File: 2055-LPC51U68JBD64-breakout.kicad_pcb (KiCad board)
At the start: 2 copper layers, 76.2 x 23.4 mm, 24 parts, among them J1 Conn_01x30, J2 Conn_01x30, J3 0548190519, U1 AZ1117CH-3.3TRG1, U2 LPC51U68

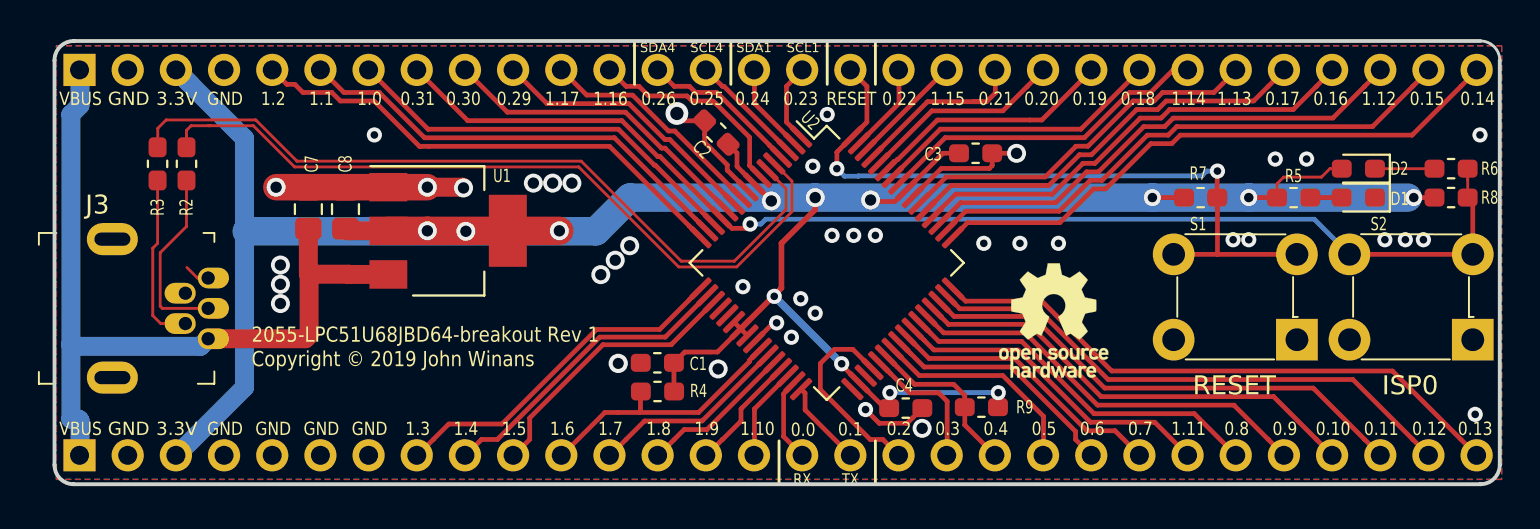
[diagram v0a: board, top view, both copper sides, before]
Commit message: Adjust edge cuts arc with wrong thickness.
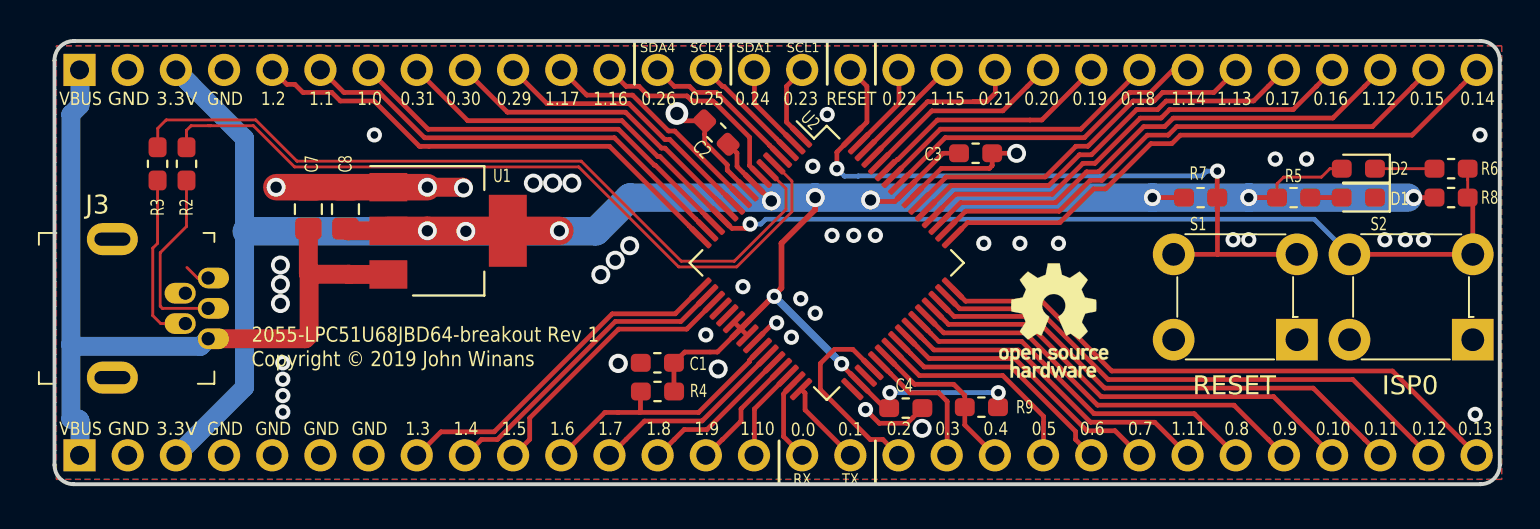
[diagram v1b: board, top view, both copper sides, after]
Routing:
- net GND: vias 41 -> 46
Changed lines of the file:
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@@
     (thickness 1.6)
     (drawings 88)
-    (tracks 528)
+    (tracks 530)
     (zones 0)
     (modules 24)
@@
     (visible_elements FFFFFF7F)
     (pcbplotparams
-      (layerselection 0x010f0_ffffffff)
+      (layerselection 0x010fc_ffffffff)
       (usegerberextensions true)
       (usegerberattributes false)
@@
   )
   (gr_arc (start 187.6044 111.76) (end 187.6044 112.776) (angle -90) (layer Edge.Cuts) (width 0.2032))
-  (gr_arc (start 187.6044 90.424) (end 188.6204 90.424) (angle -90) (layer Edge.Cuts) (width 0.15))
+  (gr_arc (start 187.6044 90.424) (end 188.6204 90.424) (angle -90) (layer Edge.Cuts) (width 0.2032))
   (gr_arc (start 113.4364 90.424) (end 113.4364 89.408) (angle -90) (layer Edge.Cuts) (width 0.2032))
   (gr_arc (start 113.4364 111.76) (end 112.4204 111.76) (angle -90) (layer Edge.Cuts) (width 0.2032))
@@
   (segment (start 120.523 101.905) (end 119.95932 101.905) (width 0.1524) (layer F.Cu) (net 1))
   (segment (start 119.95932 101.905) (end 119.40032 101.346) (width 0.1524) (layer F.Cu) (net 1))
+  (via (at 146.7612 104.902) (size 0.8) (drill 0.4) (layers F.Cu B.Cu) (net 1))
+  (via (at 124.46 106.3752) (size 0.8) (drill 0.4) (layers F.Cu B.Cu) (net 1))
+  (via (at 124.46 107.2388) (size 0.8) (drill 0.4) (layers F.Cu B.Cu) (net 1))
+  (via (at 124.46 108.1024) (size 0.8) (drill 0.4) (layers F.Cu B.Cu) (net 1))
+  (via (at 124.46 108.966) (size 0.8) (drill 0.4) (layers F.Cu B.Cu) (net 1))
   (via (at 150.2156 97.8408) (size 1) (drill 0.6) (layers F.Cu B.Cu) (net 2))
   (segment (start 156.196481 108.7628) (end 156.4272 108.7628) (width 0.25) (layer F.Cu) (net 2))
@@
   (segment (start 167.467437 96.306246) (end 169.852759 93.920924) (width 0.25) (layer F.Cu) (net 32))
   (segment (start 169.852759 93.920924) (end 170.955355 93.920924) (width 0.25) (layer F.Cu) (net 32))
+  (segment (start 167.021334 96.756256) (end 167.653838 96.756255) (width 0.25) (layer F.Cu) (net 33))
   (segment (start 165.396199 98.381391) (end 167.021334 96.756256) (width 0.25) (layer F.Cu) (net 33))
+  (segment (start 171.591765 93.920924) (end 181.910709 93.920924) (width 0.25) (layer F.Cu) (net 33))
+  (segment (start 159.437843 99.399984) (end 160.456436 98.381391) (width 0.25) (layer F.Cu) (net 33))
+  (segment (start 170.039158 94.370935) (end 171.141755 94.370935) (width 0.25) (layer F.Cu) (net 33))
   (segment (start 167.653838 96.756255) (end 170.039158 94.370935) (width 0.25) (layer F.Cu) (net 33))
-  (segment (start 167.021334 96.756256) (end 167.653838 96.756255) (width 0.25) (layer F.Cu) (net 33))
+  (segment (start 160.456436 98.381391) (end 165.396199 98.381391) (width 0.25) (layer F.Cu) (net 33))
+  (segment (start 181.910709 93.920924) (end 184.035755 91.795878) (width 0.25) (layer F.Cu) (net 33))
   (segment (start 171.141755 94.370935) (end 171.591765 93.920924) (width 0.25) (layer F.Cu) (net 33))
-  (segment (start 181.910709 93.920924) (end 184.035755 91.795878) (width 0.25) (layer F.Cu) (net 33))
   (segment (start 184.035755 91.795878) (end 184.885754 90.945879) (width 0.25) (layer F.Cu) (net 33))
-  (segment (start 159.437843 99.399984) (end 160.456436 98.381391) (width 0.25) (layer F.Cu) (net 33))
-  (segment (start 160.456436 98.381391) (end 165.396199 98.381391) (width 0.25) (layer F.Cu) (net 33))
-  (segment (start 170.039158 94.370935) (end 171.141755 94.370935) (width 0.25) (layer F.Cu) (net 33))
-  (segment (start 171.591765 93.920924) (end 181.910709 93.920924) (width 0.25) (layer F.Cu) (net 33))
+  (segment (start 167.840239 97.206264) (end 170.225557 94.820946) (width 0.25) (layer F.Cu) (net 34))
+  (segment (start 171.328155 94.820946) (end 171.778166 94.370935) (width 0.25) (layer F.Cu) (net 34))
+  (segment (start 170.225557 94.820946) (end 171.328155 94.820946) (width 0.25) (layer F.Cu) (net 34))
+  (segment (start 186.575755 91.795878) (end 187.425754 90.945879) (width 0.25) (layer F.Cu) (net 34))
+  (segment (start 171.778166 94.370935) (end 184.000698 94.370935) (width 0.25) (layer F.Cu) (net 34))
+  (segment (start 184.000698 94.370935) (end 186.575755 91.795878) (width 0.25) (layer F.Cu) (net 34))
   (segment (start 167.207735 97.206265) (end 167.840239 97.206264) (width 0.25) (layer F.Cu) (net 34))
-  (segment (start 171.778166 94.370935) (end 184.000698 94.370935) (width 0.25) (layer F.Cu) (net 34))
-  (segment (start 186.575755 91.795878) (end 187.425754 90.945879) (width 0.25) (layer F.Cu) (net 34))
-  (segment (start 171.328155 94.820946) (end 171.778166 94.370935) (width 0.25) (layer F.Cu) (net 34))
-  (segment (start 184.000698 94.370935) (end 186.575755 91.795878) (width 0.25) (layer F.Cu) (net 34))
   (segment (start 159.791397 99.753537) (end 160.561134 98.9838) (width 0.25) (layer F.Cu) (net 34))
+  (segment (start 165.4302 98.9838) (end 167.207735 97.206265) (width 0.25) (layer F.Cu) (net 34))
   (segment (start 160.561134 98.9838) (end 165.4302 98.9838) (width 0.25) (layer F.Cu) (net 34))
-  (segment (start 165.4302 98.9838) (end 167.207735 97.206265) (width 0.25) (layer F.Cu) (net 34))
-  (segment (start 167.840239 97.206264) (end 170.225557 94.820946) (width 0.25) (layer F.Cu) (net 34))
-  (segment (start 170.225557 94.820946) (end 171.328155 94.820946) (width 0.25) (layer F.Cu) (net 34))
   (segment (start 182.966875 106.807) (end 186.575755 110.41588) (width 0.25) (layer F.Cu) (net 35))
   (segment (start 159.791397 102.458221) (end 160.457176 103.124) (width 0.25) (layer F.Cu) (net 35))
@@
   (segment (start 142.555753 110.41588) (end 141.705754 111.265879) (width 0.25) (layer F.Cu) (net 50))
   (segment (start 137.475753 110.41588) (end 136.625754 111.265879) (width 0.25) (layer F.Cu) (net 51))
-  (segment (start 144.931524 105.421022) (end 141.334898 105.421022) (width 0.25) (layer F.Cu) (net 51))
-  (segment (start 141.334898 105.421022) (end 137.475753 109.280167) (width 0.25) (layer F.Cu) (net 51))
   (segment (start 137.475753 109.280167) (end 137.475753 110.41588) (width 0.25) (layer F.Cu) (net 51))
-  (segment (start 147.187218 103.165328) (end 144.931524 105.421022) (width 0.25) (layer F.Cu) (net 51))
+  (segment (start 142.15872 104.5972) (end 137.475753 109.280167) (width 0.25) (layer F.Cu) (net 51))
+  (segment (start 145.755346 104.5972) (end 142.15872 104.5972) (width 0.25) (layer F.Cu) (net 51))
+  (segment (start 147.187218 103.165328) (end 145.755346 104.5972) (width 0.25) (layer F.Cu) (net 51))
+  (segment (start 135.770945 110.41588) (end 134.935753 110.41588) (width 0.25) (layer F.Cu) (net 52))
   (segment (start 134.935753 110.41588) (end 134.085754 111.265879) (width 0.25) (layer F.Cu) (net 52))
-  (segment (start 141.168214 105.018611) (end 135.770945 110.41588) (width 0.25) (layer F.Cu) (net 52))
-  (segment (start 144.626828 105.018611) (end 141.168214 105.018611) (width 0.25) (layer F.Cu) (net 52))
-  (segment (start 146.833665 102.811774) (end 144.626828 105.018611) (width 0.25) (layer F.Cu) (net 52))
-  (segment (start 135.770945 110.41588) (end 134.935753 110.41588) (width 0.25) (layer F.Cu) (net 52))
-  (segment (start 145.88791 103.050422) (end 145.88791 103.05749) (width 0.25) (layer F.Cu) (net 53))
-  (segment (start 133.210633 109.601) (end 132.395753 110.41588) (width 0.25) (layer F.Cu) (net 53))
-  (segment (start 145.88791 103.05749) (end 144.3292 104.6162) (width 0.25) (layer F.Cu) (net 53))
-  (segment (start 144.3292 104.6162) (end 141.00153 104.6162) (width 0.25) (layer F.Cu) (net 53))
-  (segment (start 141.00153 104.6162) (end 136.01673 109.601) (width 0.25) (layer F.Cu) (net 53))
-  (segment (start 136.01673 109.601) (end 133.210633 109.601) (width 0.25) (layer F.Cu) (net 53))
-  (segment (start 146.480111 102.458221) (end 145.88791 103.050422) (width 0.25) (layer F.Cu) (net 53))
-  (segment (start 132.395753 110.41588) (end 131.545754 111.265879) (width 0.25) (layer F.Cu) (net 53))
+  (segment (start 145.45065 104.194789) (end 141.992036 104.194789) (width 0.25) (layer F.Cu) (net 52))
+  (segment (start 141.992036 104.194789) (end 135.770945 110.41588) (width 0.25) (layer F.Cu) (net 52))
+  (segment (start 146.833665 102.811774) (end 145.45065 104.194789) (width 0.25) (layer F.Cu) (net 52))
+  (segment (start 132.798163 110.01347) (end 131.545754 111.265879) (width 0.25) (layer F.Cu) (net 53))
+  (segment (start 135.604262 110.01347) (end 132.798163 110.01347) (width 0.25) (layer F.Cu) (net 53))
+  (segment (start 141.825353 103.792379) (end 135.604262 110.01347) (width 0.25) (layer F.Cu) (net 53))
+  (segment (start 146.480111 102.458221) (end 145.145953 103.792379) (width 0.25) (layer F.Cu) (net 53))
+  (segment (start 145.145953 103.792379) (end 141.825353 103.792379) (width 0.25) (layer F.Cu) (net 53))
   (segment (start 119.38 94.385) (end 119.37746 94.38246) (width 0.1524) (layer F.Cu) (net 54))
   (segment (start 119.38 95.01) (end 119.38 94.385) (width 0.1524) (layer F.Cu) (net 54))

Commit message: Fix rev number on front silkscreen
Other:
- board text added: "2055-LPC51U68JBD64-breakout Rev 2 Copyright © 2019 John Winans"
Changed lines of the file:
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@@
     (effects (font (size 0.7 0.6) (thickness 0.125)))
   )
-  (gr_text "2055-LPC51U68JBD64-breakout Rev 1\nCopyright © 2019 John Winans" (at 122.809 105.537) (layer F.SilkS)
+  (gr_text "2055-LPC51U68JBD64-breakout Rev 2\nCopyright © 2019 John Winans" (at 122.809 105.537) (layer F.SilkS)
     (effects (font (size 0.8 0.7) (thickness 0.175)) (justify left))
   )

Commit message: Fix rev number on back silkscreen
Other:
- board text removed: "2055-LPC51U68JBD64-breakout Rev 1 Copyright © 2019 John Winans"
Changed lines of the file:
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@@
     (effects (font (size 0.7 0.6) (thickness 0.125)))
   )
-  (gr_text "2055-LPC51U68JBD64-breakout Rev 1\nCopyright © 2019 John Winans\n" (at 186.944 94.488) (layer B.SilkS)
+  (gr_text "2055-LPC51U68JBD64-breakout Rev 2\nCopyright © 2019 John Winans\n" (at 186.944 94.488) (layer B.SilkS)
     (effects (font (size 1.2 0.8) (thickness 0.2)) (justify left mirror))
   )

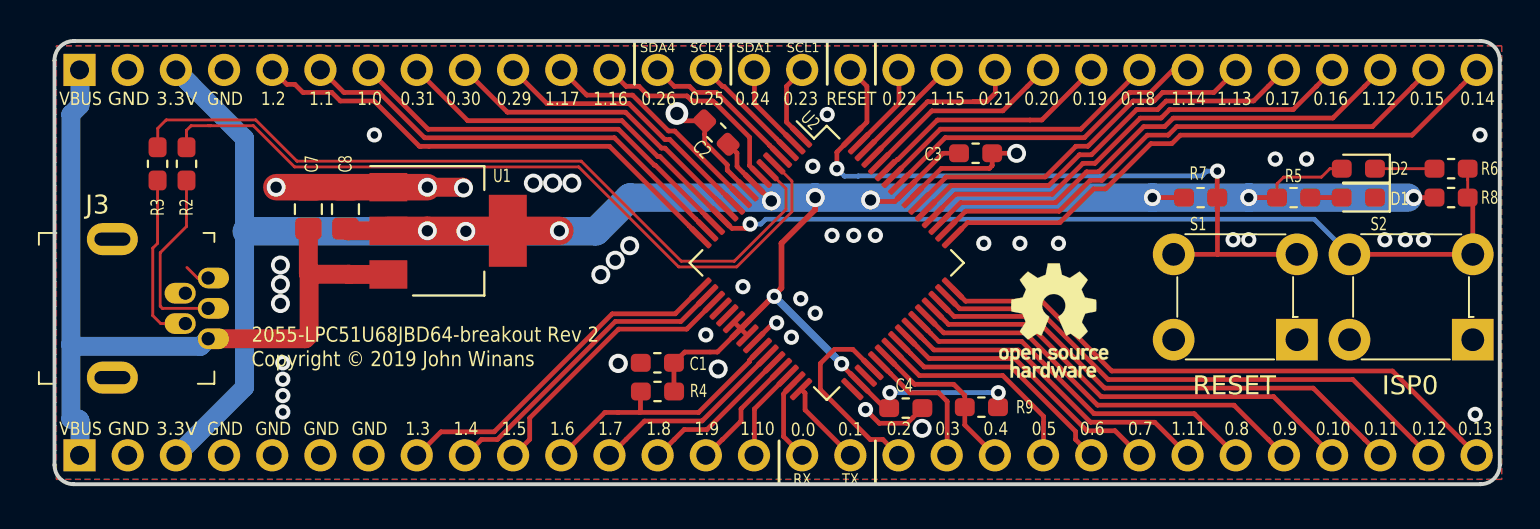
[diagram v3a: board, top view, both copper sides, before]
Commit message: Reverse J3 pin order.
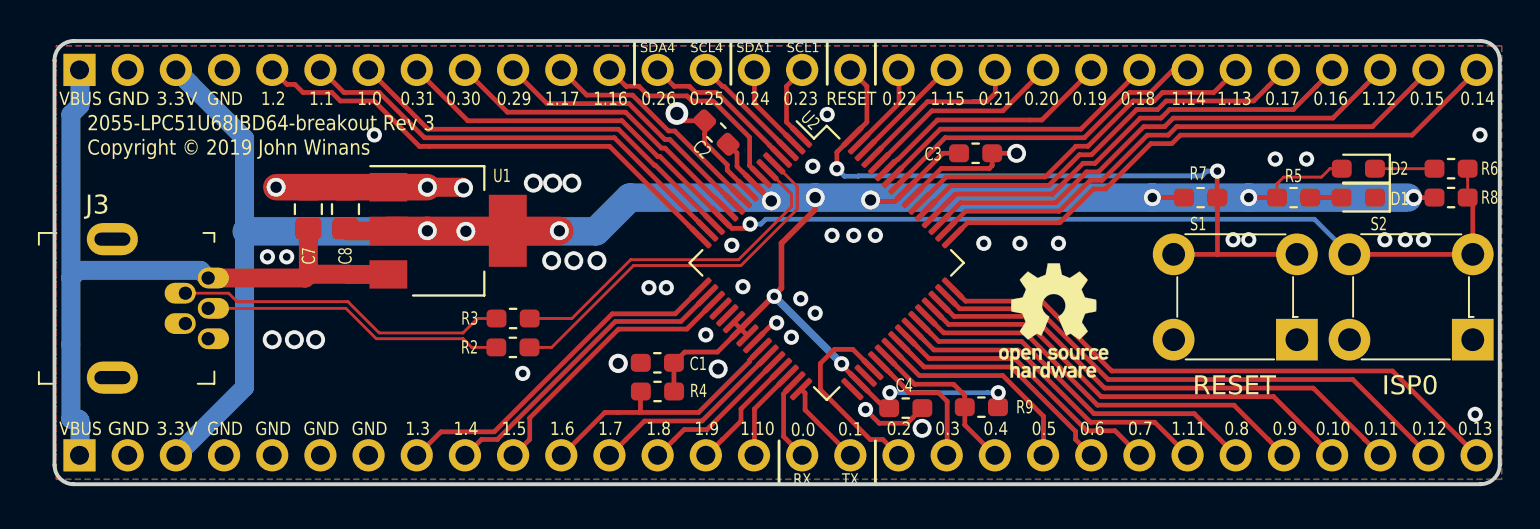
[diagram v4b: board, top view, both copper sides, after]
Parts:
- moved R3 20.4 mm to (136.6, 104.0), turned to 0 degrees
- moved R2 19.7 mm to (136.6, 105.6), turned to 0 degrees
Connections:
- J3 pad 1: /VBUS -> GND
- J3 pad 5: GND -> /VBUS
- R3 pad 1: Net-(J3-Pad2) -> Net-(J3-Pad4)
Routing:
- net /USB_DM: track 41.0 -> 18.7 mm
- net /USB_DP: track 40.3 -> 20.1 mm
- net Net-(J3-Pad4): track 0.00 -> 17.6 mm
- net Net-(J3-Pad2): track 9.13 -> 0.00 mm
- net Net-(J3-Pad3): track 9.78 -> 16.0 mm
- net /VBUS: track 43.6 -> 40.5 mm
- net GND: track 37.5 -> 36.2 mm, vias 46 -> 48
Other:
- board text added: "2055-LPC51U68JBD64-breakout Rev 3 Copyright © 2019 John Winans"
- board text removed: "2055-LPC51U68JBD64-breakout Rev 2 Copyright © 2019 John Winans"

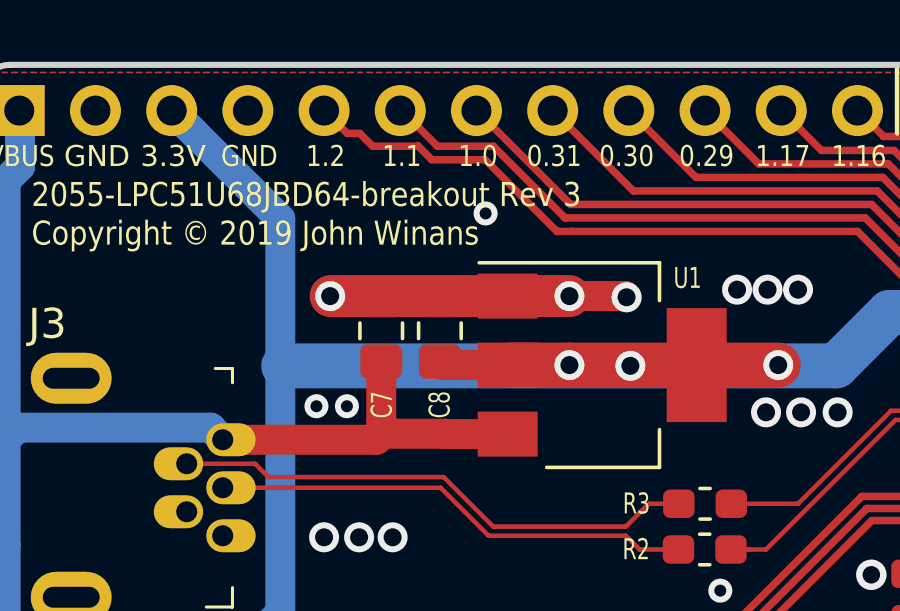
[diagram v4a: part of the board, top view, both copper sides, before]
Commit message: Correct thermal releif around C7 & C8.
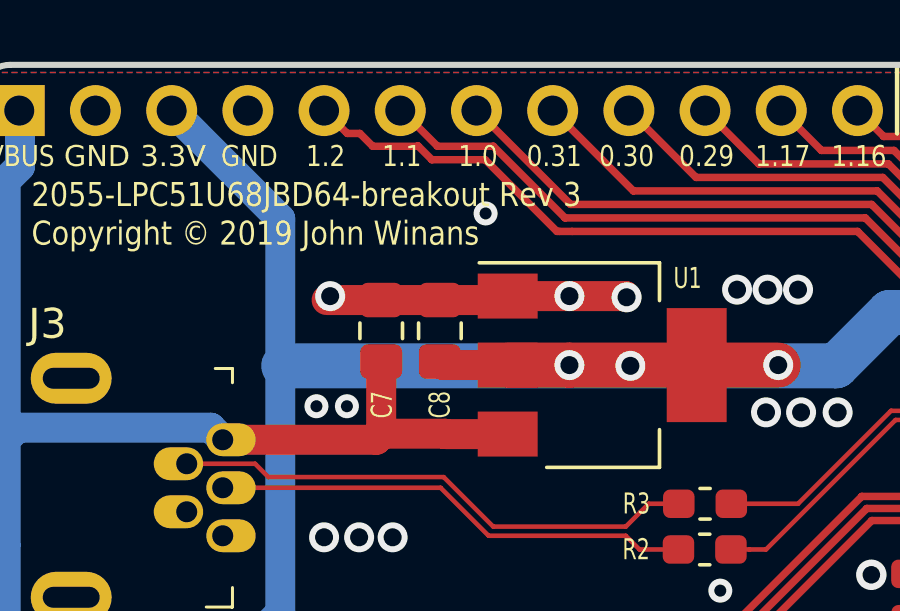
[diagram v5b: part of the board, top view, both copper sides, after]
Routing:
- net GND: track 36.2 -> 28.2 mm
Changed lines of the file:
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@@
-(kicad_pcb (version 20171130) (host pcbnew 5.1.2-f72e74a~84~ubuntu18.04.1)
+(kicad_pcb (version 20171130) (host pcbnew 5.1.3-ffb9f22~84~ubuntu18.04.1)
   (general
     (thickness 1.6)
     (drawings 88)
-    (tracks 520)
+    (tracks 519)
     (zones 0)
     (modules 24)
@@
   (via (at 178.435 95.631) (size 0.8) (drill 0.4) (layers F.Cu B.Cu) (net 1))
   (via (at 187.579 94.361) (size 0.8) (drill 0.4) (layers F.Cu B.Cu) (net 1))
-  (segment (start 127.894 97.1156) (end 127.762 97.2476) (width 1) (layer F.Cu) (net 1))
-  (segment (start 130.0222 97.1156) (end 127.894 97.1156) (width 1) (layer F.Cu) (net 1))
   (segment (start 127.762 97.2476) (end 125.8062 97.2476) (width 1) (layer F.Cu) (net 1))
   (via (at 147.41144 106.69778) (size 1) (drill 0.6) (layers F.Cu B.Cu) (net 1))
@@
   (segment (start 133.9456 97.1156) (end 133.985 97.155) (width 1) (layer F.Cu) (net 1))
   (via (at 124.1044 97.1169) (size 1) (drill 0.6) (layers F.Cu B.Cu) (net 1))
-  (segment (start 132.079998 97.1156) (end 124.1184 97.1156) (width 1.4) (layer F.Cu) (net 1))
   (via (at 150.495 104.267) (size 0.8) (drill 0.4) (layers F.Cu B.Cu) (net 1))
   (segment (start 149.308539 105.286648) (end 150.328187 104.267) (width 0.25) (layer F.Cu) (net 1))
@@
   (via (at 148.1328 100.1776) (size 0.8) (drill 0.4) (layers F.Cu B.Cu) (net 1))
   (via (at 137.1092 106.934) (size 0.8) (drill 0.4) (layers F.Cu B.Cu) (net 1))
+  (segment (start 129.8902 97.2476) (end 127.762 97.2476) (width 1) (layer F.Cu) (net 1))
+  (segment (start 130.0222 97.1156) (end 129.8902 97.2476) (width 1) (layer F.Cu) (net 1))
   (via (at 150.2156 97.8408) (size 1) (drill 0.6) (layers F.Cu B.Cu) (net 2))
   (segment (start 156.196481 108.7628) (end 156.4272 108.7628) (width 0.25) (layer F.Cu) (net 2))

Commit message: Clean up Digikey order numbers in the BOM.
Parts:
- U1: value AZ1117CH-3.3TRG1 -> AZ1117CH-3.3TRG1
- U2: value LPC51U68 -> LPC51U68JBD64QL
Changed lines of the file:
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@@
       (effects (font (size 0.7 0.5) (thickness 0.125)))
     )
-    (fp_text value LPC51U68 (at 0 7.35 315) (layer F.Fab)
+    (fp_text value LPC51U68JBD64QL (at 0 7.35 315) (layer F.Fab)
       (effects (font (size 1 1) (thickness 0.15)))
     )
@@
       (effects (font (size 0.7 0.5) (thickness 0.125)))
     )
-    (fp_text value " AZ1117CH-3.3TRG1" (at 0 4.5) (layer F.Fab)
-      (effects (font (size 1 1) (thickness 0.15)))
-    )
+    (fp_text value AZ1117CH-3.3TRG1 (at 0 4.5) (layer F.Fab)
+      (effects (font (size 1 1) (thickness 0.15)))
+    )
